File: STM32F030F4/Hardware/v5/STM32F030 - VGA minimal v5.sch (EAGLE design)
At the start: 28 parts, among them Q1 3904, U1 MCP1700/TT, U2 STM32F030F4P6, X1 25MHz

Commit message: ChibiTerm source snapshot take 3
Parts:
- LICENSE: PARTNO * -> LICENSE
- R1: PARTNO 10K, 0603 -> 4K7, 0603
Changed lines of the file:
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@@
 <part name="SUPPLY10" library="supply2" deviceset="GND" device=""/>
 <part name="R1" library="ipc-7351-resistor" deviceset="RESISTOR_" device="0603" value="4K7">
-<attribute name="PARTNO" value="10K, 0603"/>
+<attribute name="PARTNO" value="4K7, 0603"/>
 </part>
 <part name="C4" library="ipc-7351-capacitor" deviceset="CAPACITOR_" device="0603" value="0.1uF">
@@
 </part>
 <part name="LICENSE" library="Misc logo" deviceset="CC-BY-NC" device="75%" value="CC-BY-NC">
-<attribute name="PARTNO" value="*"/>
+<attribute name="PARTNO" value="LICENSE"/>
 </part>
 <part name="X1" library="crystal" deviceset="CRYSTAL" device="SM49" value="25MHz">

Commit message: ChibiTerm source snapshot take 4
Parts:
- R7: PARTNO 330R, 0603 -> 475R, 0603
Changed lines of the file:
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@@
 </part>
 <part name="R7" library="ipc-7351-resistor" deviceset="RESISTOR_" device="0603" value="475R">
-<attribute name="PARTNO" value="330R, 0603"/>
+<attribute name="PARTNO" value="475R, 0603"/>
 </part>
 <part name="SUPPLY4" library="Misc Voltages" deviceset="+3.3V" device=""/>

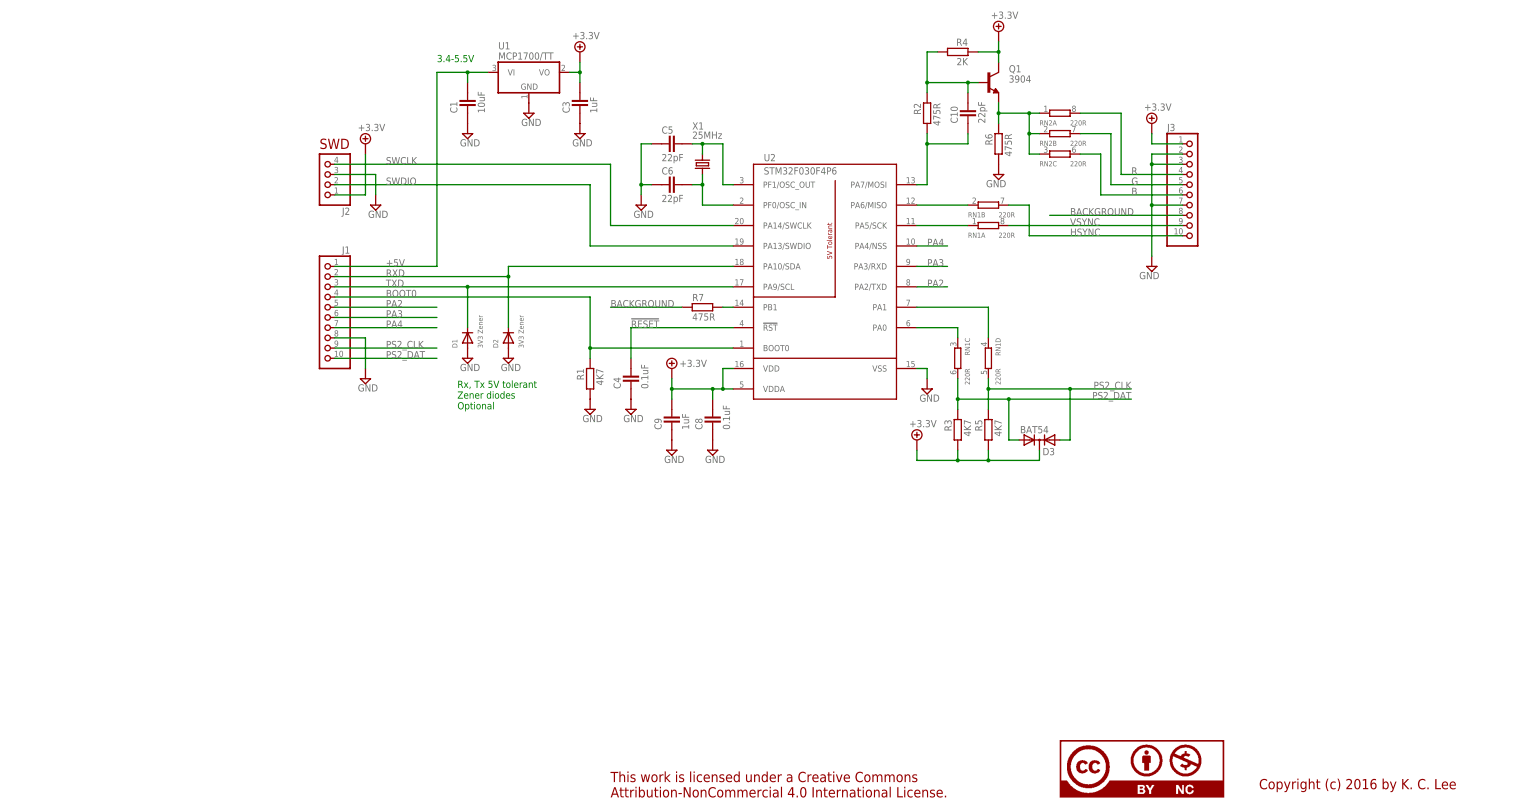
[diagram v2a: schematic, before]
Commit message: Zener diodes value change
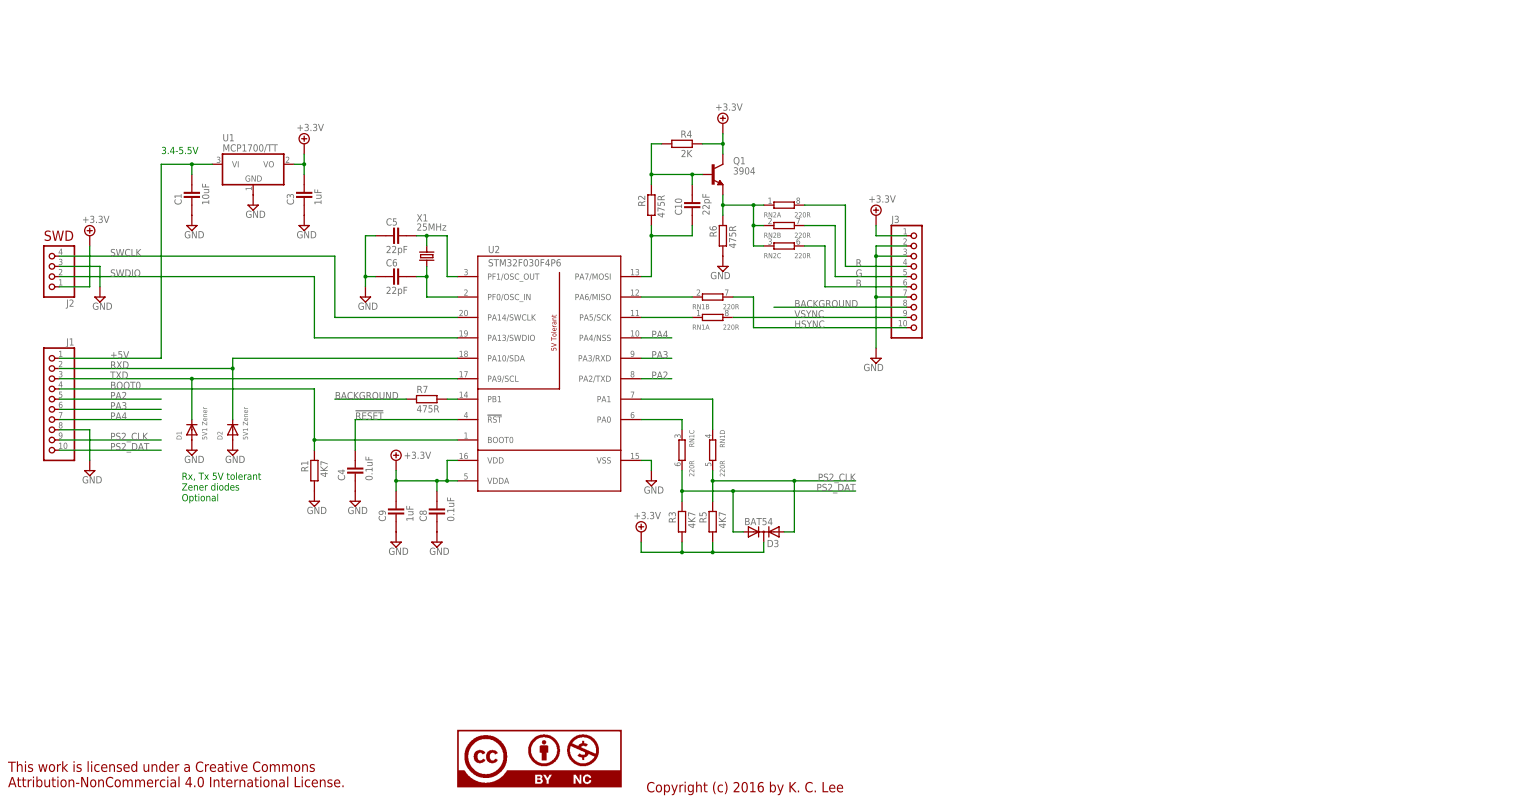
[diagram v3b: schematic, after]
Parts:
- D1, D2: value 3V3 Zener -> 5V1 Zener; PARTNO BZT52C3V3 -> BZT52C5V1
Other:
- moved on the sheet: C1, C10, C3, C4, C5, C6, C8, C9, D1, D2, D3, J1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
